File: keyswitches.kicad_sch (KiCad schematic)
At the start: 16 parts

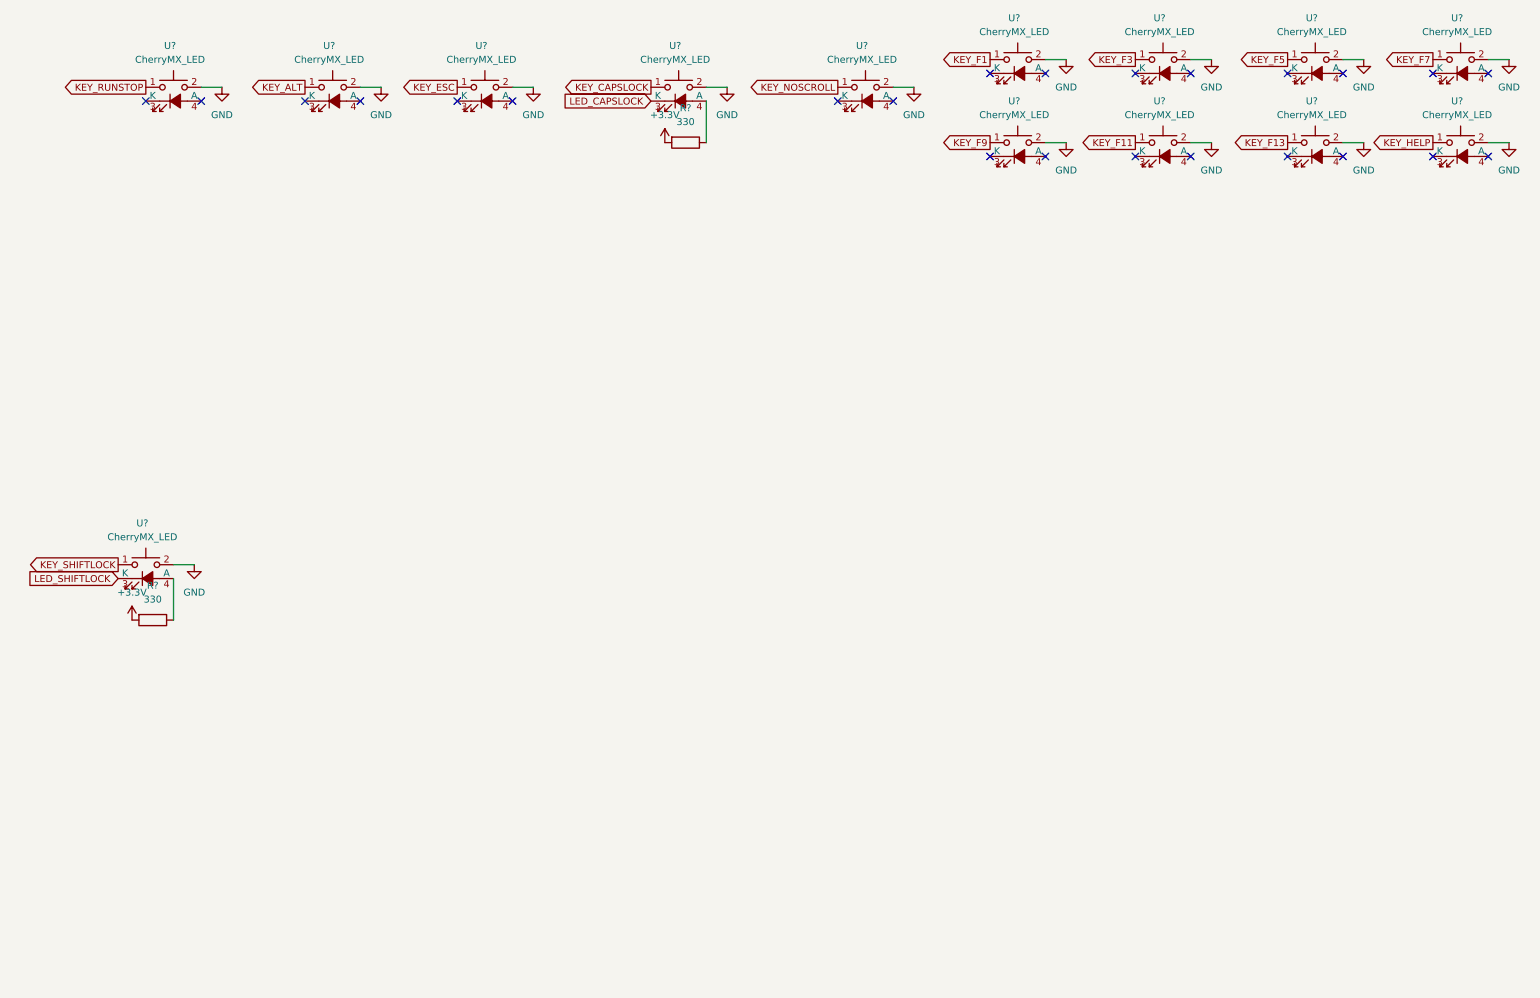
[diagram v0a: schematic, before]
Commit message: place top row of key switches
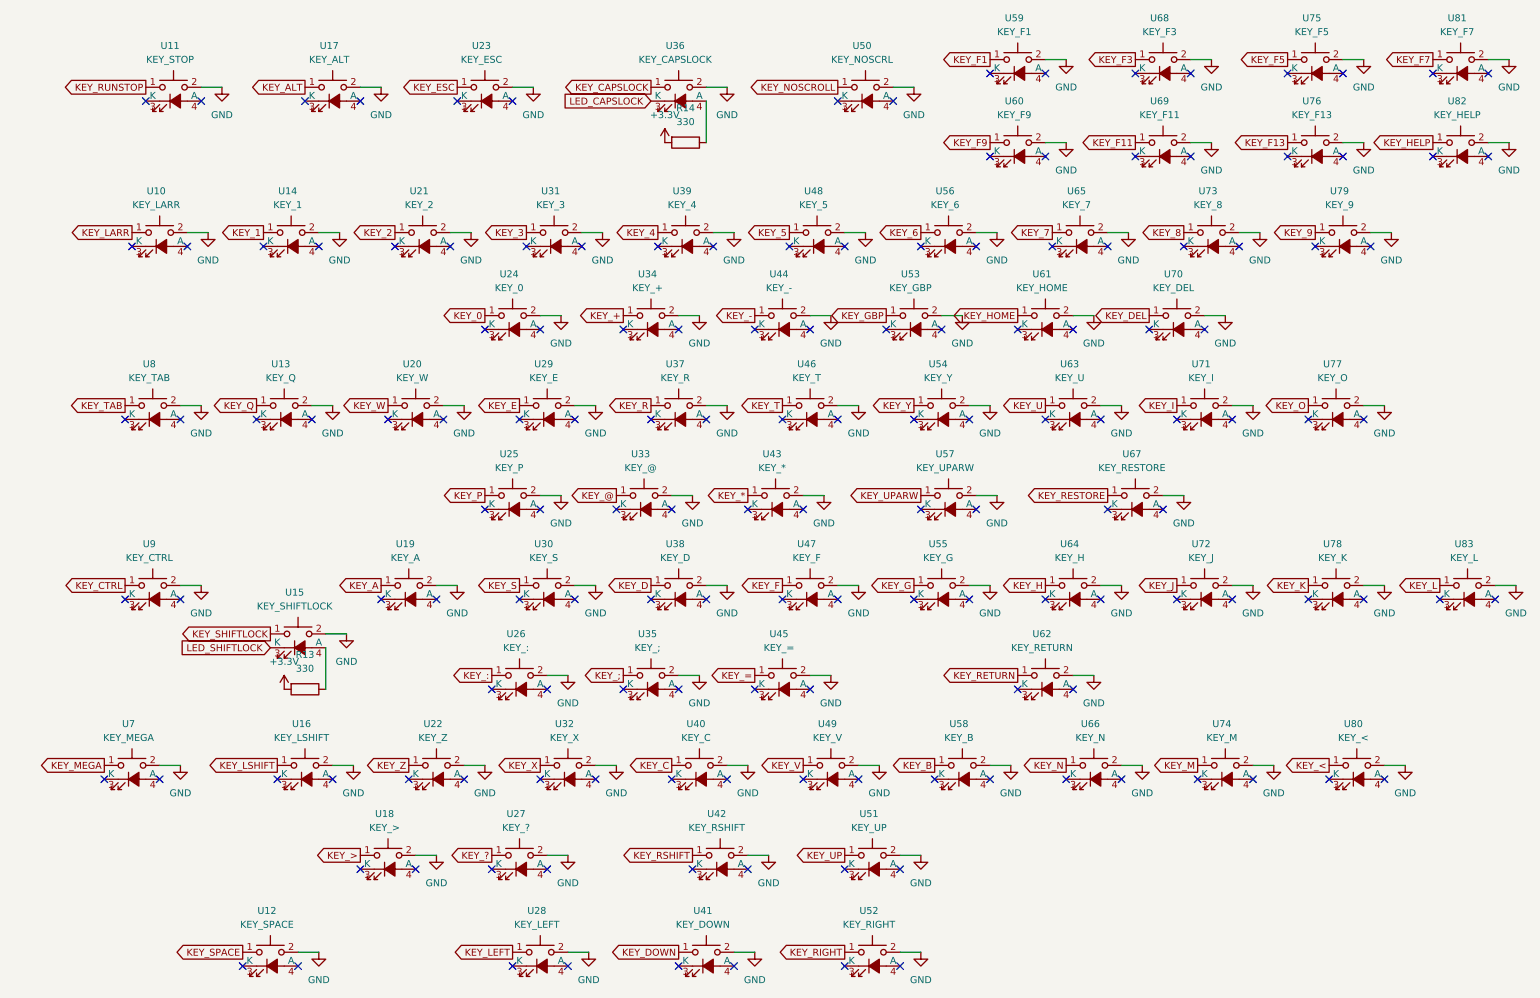
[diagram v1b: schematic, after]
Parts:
- added U10: KEY_LARR, 00Project-KeySwitches:SW_Cherry_MX1A_1.00u_PCB_LED, symbol 00Project-CherryMX:CherryMX_LED
- added U12: KEY_SPACE, 00Project-KeySwitches:SW_Cherry_MX1A_1.00u_PCB_LED, symbol 00Project-CherryMX:CherryMX_LED
- added U13: KEY_Q, 00Project-KeySwitches:SW_Cherry_MX1A_1.00u_PCB_LED, symbol 00Project-CherryMX:CherryMX_LED
- added U14: KEY_1, 00Project-KeySwitches:SW_Cherry_MX1A_1.00u_PCB_LED, symbol 00Project-CherryMX:CherryMX_LED
- added U16: KEY_LSHIFT, 00Project-KeySwitches:SW_Cherry_MX1A_1.00u_PCB_LED, symbol 00Project-CherryMX:CherryMX_LED
- added U18: KEY_>, 00Project-KeySwitches:SW_Cherry_MX1A_1.00u_PCB_LED, symbol 00Project-CherryMX:CherryMX_LED
- added U19: KEY_A, 00Project-KeySwitches:SW_Cherry_MX1A_1.00u_PCB_LED, symbol 00Project-CherryMX:CherryMX_LED
- added U20: KEY_W, 00Project-KeySwitches:SW_Cherry_MX1A_1.00u_PCB_LED, symbol 00Project-CherryMX:CherryMX_LED
- added U21: KEY_2, 00Project-KeySwitches:SW_Cherry_MX1A_1.00u_PCB_LED, symbol 00Project-CherryMX:CherryMX_LED
- added U22: KEY_Z, 00Project-KeySwitches:SW_Cherry_MX1A_1.00u_PCB_LED, symbol 00Project-CherryMX:CherryMX_LED
- added U24: KEY_0, 00Project-KeySwitches:SW_Cherry_MX1A_1.00u_PCB_LED, symbol 00Project-CherryMX:CherryMX_LED
- added U25: KEY_P, 00Project-KeySwitches:SW_Cherry_MX1A_1.00u_PCB_LED, symbol 00Project-CherryMX:CherryMX_LED
- added U26: KEY_:, 00Project-KeySwitches:SW_Cherry_MX1A_1.00u_PCB_LED, symbol 00Project-CherryMX:CherryMX_LED
- added U27: KEY_?, 00Project-KeySwitches:SW_Cherry_MX1A_1.00u_PCB_LED, symbol 00Project-CherryMX:CherryMX_LED
- added U28: KEY_LEFT, 00Project-KeySwitches:SW_Cherry_MX1A_1.00u_PCB_LED, symbol 00Project-CherryMX:CherryMX_LED
- added U29: KEY_E, 00Project-KeySwitches:SW_Cherry_MX1A_1.00u_PCB_LED, symbol 00Project-CherryMX:CherryMX_LED
- added U30: KEY_S, 00Project-KeySwitches:SW_Cherry_MX1A_1.00u_PCB_LED, symbol 00Project-CherryMX:CherryMX_LED
- added U31: KEY_3, 00Project-KeySwitches:SW_Cherry_MX1A_1.00u_PCB_LED, symbol 00Project-CherryMX:CherryMX_LED
- added U32: KEY_X, 00Project-KeySwitches:SW_Cherry_MX1A_1.00u_PCB_LED, symbol 00Project-CherryMX:CherryMX_LED
- added U33: KEY_@, 00Project-KeySwitches:SW_Cherry_MX1A_1.00u_PCB_LED, symbol 00Project-CherryMX:CherryMX_LED
- added U34: KEY_+, 00Project-KeySwitches:SW_Cherry_MX1A_1.00u_PCB_LED, symbol 00Project-CherryMX:CherryMX_LED
- added U35: KEY_;, 00Project-KeySwitches:SW_Cherry_MX1A_1.00u_PCB_LED, symbol 00Project-CherryMX:CherryMX_LED
- added U37: KEY_R, 00Project-KeySwitches:SW_Cherry_MX1A_1.00u_PCB_LED, symbol 00Project-CherryMX:CherryMX_LED
- added U38: KEY_D, 00Project-KeySwitches:SW_Cherry_MX1A_1.00u_PCB_LED, symbol 00Project-CherryMX:CherryMX_LED
- added U39: KEY_4, 00Project-KeySwitches:SW_Cherry_MX1A_1.00u_PCB_LED, symbol 00Project-CherryMX:CherryMX_LED
- added U40: KEY_C, 00Project-KeySwitches:SW_Cherry_MX1A_1.00u_PCB_LED, symbol 00Project-CherryMX:CherryMX_LED
- added U41: KEY_DOWN, 00Project-KeySwitches:SW_Cherry_MX1A_1.00u_PCB_LED, symbol 00Project-CherryMX:CherryMX_LED
- added U42: KEY_RSHIFT, 00Project-KeySwitches:SW_Cherry_MX1A_1.00u_PCB_LED, symbol 00Project-CherryMX:CherryMX_LED
- added U43: KEY_*, 00Project-KeySwitches:SW_Cherry_MX1A_1.00u_PCB_LED, symbol 00Project-CherryMX:CherryMX_LED
- added U44: KEY_-, 00Project-KeySwitches:SW_Cherry_MX1A_1.00u_PCB_LED, symbol 00Project-CherryMX:CherryMX_LED
- added U45: KEY_=, 00Project-KeySwitches:SW_Cherry_MX1A_1.00u_PCB_LED, symbol 00Project-CherryMX:CherryMX_LED
- added U46: KEY_T, 00Project-KeySwitches:SW_Cherry_MX1A_1.00u_PCB_LED, symbol 00Project-CherryMX:CherryMX_LED
- added U47: KEY_F, 00Project-KeySwitches:SW_Cherry_MX1A_1.00u_PCB_LED, symbol 00Project-CherryMX:CherryMX_LED
- added U48: KEY_5, 00Project-KeySwitches:SW_Cherry_MX1A_1.00u_PCB_LED, symbol 00Project-CherryMX:CherryMX_LED
- added U49: KEY_V, 00Project-KeySwitches:SW_Cherry_MX1A_1.00u_PCB_LED, symbol 00Project-CherryMX:CherryMX_LED
- added U51: KEY_UP, 00Project-KeySwitches:SW_Cherry_MX1A_1.00u_PCB_LED, symbol 00Project-CherryMX:CherryMX_LED
- added U52: KEY_RIGHT, 00Project-KeySwitches:SW_Cherry_MX1A_1.00u_PCB_LED, symbol 00Project-CherryMX:CherryMX_LED
- added U53: KEY_GBP, 00Project-KeySwitches:SW_Cherry_MX1A_1.00u_PCB_LED, symbol 00Project-CherryMX:CherryMX_LED
- added U54: KEY_Y, 00Project-KeySwitches:SW_Cherry_MX1A_1.00u_PCB_LED, symbol 00Project-CherryMX:CherryMX_LED
- added U55: KEY_G, 00Project-KeySwitches:SW_Cherry_MX1A_1.00u_PCB_LED, symbol 00Project-CherryMX:CherryMX_LED
- added U56: KEY_6, 00Project-KeySwitches:SW_Cherry_MX1A_1.00u_PCB_LED, symbol 00Project-CherryMX:CherryMX_LED
- added U57: KEY_UPARW, 00Project-KeySwitches:SW_Cherry_MX1A_1.00u_PCB_LED, symbol 00Project-CherryMX:CherryMX_LED
- added U58: KEY_B, 00Project-KeySwitches:SW_Cherry_MX1A_1.00u_PCB_LED, symbol 00Project-CherryMX:CherryMX_LED
- added U61: KEY_HOME, 00Project-KeySwitches:SW_Cherry_MX1A_1.00u_PCB_LED, symbol 00Project-CherryMX:CherryMX_LED
- added U62: KEY_RETURN, 00Project-KeySwitches:SW_Cherry_MX1A_1.00u_PCB_LED, symbol 00Project-CherryMX:CherryMX_LED
- added U63: KEY_U, 00Project-KeySwitches:SW_Cherry_MX1A_1.00u_PCB_LED, symbol 00Project-CherryMX:CherryMX_LED
- added U64: KEY_H, 00Project-KeySwitches:SW_Cherry_MX1A_1.00u_PCB_LED, symbol 00Project-CherryMX:CherryMX_LED
- added U65: KEY_7, 00Project-KeySwitches:SW_Cherry_MX1A_1.00u_PCB_LED, symbol 00Project-CherryMX:CherryMX_LED
- added U66: KEY_N, 00Project-KeySwitches:SW_Cherry_MX1A_1.00u_PCB_LED, symbol 00Project-CherryMX:CherryMX_LED
- added U67: KEY_RESTORE, 00Project-KeySwitches:SW_Cherry_MX1A_1.00u_PCB_LED, symbol 00Project-CherryMX:CherryMX_LED
- added U7: KEY_MEGA, 00Project-KeySwitches:SW_Cherry_MX1A_1.00u_PCB_LED, symbol 00Project-CherryMX:CherryMX_LED
- added U70: KEY_DEL, 00Project-KeySwitches:SW_Cherry_MX1A_1.00u_PCB_LED, symbol 00Project-CherryMX:CherryMX_LED
- added U71: KEY_I, 00Project-KeySwitches:SW_Cherry_MX1A_1.00u_PCB_LED, symbol 00Project-CherryMX:CherryMX_LED
- added U72: KEY_J, 00Project-KeySwitches:SW_Cherry_MX1A_1.00u_PCB_LED, symbol 00Project-CherryMX:CherryMX_LED
- added U73: KEY_8, 00Project-KeySwitches:SW_Cherry_MX1A_1.00u_PCB_LED, symbol 00Project-CherryMX:CherryMX_LED
- added U74: KEY_M, 00Project-KeySwitches:SW_Cherry_MX1A_1.00u_PCB_LED, symbol 00Project-CherryMX:CherryMX_LED
- added U77: KEY_O, 00Project-KeySwitches:SW_Cherry_MX1A_1.00u_PCB_LED, symbol 00Project-CherryMX:CherryMX_LED
- added U78: KEY_K, 00Project-KeySwitches:SW_Cherry_MX1A_1.00u_PCB_LED, symbol 00Project-CherryMX:CherryMX_LED
- added U79: KEY_9, 00Project-KeySwitches:SW_Cherry_MX1A_1.00u_PCB_LED, symbol 00Project-CherryMX:CherryMX_LED
- added U8: KEY_TAB, 00Project-KeySwitches:SW_Cherry_MX1A_1.00u_PCB_LED, symbol 00Project-CherryMX:CherryMX_LED
- added U80: KEY_<, 00Project-KeySwitches:SW_Cherry_MX1A_1.00u_PCB_LED, symbol 00Project-CherryMX:CherryMX_LED
- added U83: KEY_L, 00Project-KeySwitches:SW_Cherry_MX1A_1.00u_PCB_LED, symbol 00Project-CherryMX:CherryMX_LED
- added U9: KEY_CTRL, 00Project-KeySwitches:SW_Cherry_MX1A_1.00u_PCB_LED, symbol 00Project-CherryMX:CherryMX_LED
- U11: renamed from U?; value CherryMX_LED -> KEY_STOP
- U15: renamed from U?; value CherryMX_LED -> KEY_SHIFTLOCK
- U17: renamed from U?; value CherryMX_LED -> KEY_ALT
- U23: renamed from U?; value CherryMX_LED -> KEY_ESC
- U36: renamed from U?; value CherryMX_LED -> KEY_CAPSLOCK
- U50: renamed from U?; value CherryMX_LED -> KEY_NOSCRL
- U59: renamed from U?; value CherryMX_LED -> KEY_F1
- U60: renamed from U?; value CherryMX_LED -> KEY_F9
- U68: renamed from U?; value CherryMX_LED -> KEY_F3
- U69: renamed from U?; value CherryMX_LED -> KEY_F11
- U75: renamed from U?; value CherryMX_LED -> KEY_F5
- U76: renamed from U?; value CherryMX_LED -> KEY_F13
- U81: renamed from U?; value CherryMX_LED -> KEY_F7
- U82: renamed from U?; value CherryMX_LED -> KEY_HELP
- gave numbers to parts that had none: 2
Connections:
- net GND: now also U10.2, U12.2, U13.2, U14.2, U16.2, U18.2, U19.2, U20.2, U21.2, U22.2, U24.2, U25.2, U26.2, U27.2, U28.2, U29.2, U30.2, U31.2, U32.2, U33.2, U34.2, U35.2, U37.2, U38.2, U39.2, U40.2, U41.2, U42.2, U43.2, U44.2, U45.2, U46.2, U47.2, U48.2, U49.2, U51.2, U52.2, U53.2, U54.2, U55.2, U56.2, U57.2, U58.2, U61.2, U62.2, U63.2, U64.2, U65.2, U66.2, U67.2, U7.2, U70.2, U71.2, U72.2, U73.2, U74.2, U77.2, U78.2, U79.2, U8.2, U80.2, U83.2, U9.2
- new net KEY_*: U43.1
- new net KEY_+: U34.1
- new net KEY_-: U44.1
- new net KEY_0: U24.1
- new net KEY_1: U14.1
- new net KEY_2: U21.1
- new net KEY_3: U31.1
- new net KEY_4: U39.1
- new net KEY_5: U48.1
- new net KEY_6: U56.1
- new net KEY_7: U65.1
- new net KEY_8: U73.1
- new net KEY_9: U79.1
- new net KEY_:: U26.1
- new net KEY_;: U35.1
- new net KEY_<: U80.1
- new net KEY_=: U45.1
- new net KEY_>: U18.1
- new net KEY_?: U27.1
- new net KEY_@: U33.1
- new net KEY_A: U19.1
- new net KEY_B: U58.1
- new net KEY_C: U40.1
- new net KEY_CTRL: U9.1
- new net KEY_D: U38.1
- new net KEY_DEL: U70.1
- new net KEY_DOWN: U41.1
- new net KEY_E: U29.1
- new net KEY_F: U47.1
- new net KEY_G: U55.1
- new net KEY_GBP: U53.1
- new net KEY_H: U64.1
- new net KEY_HOME: U61.1
- new net KEY_I: U71.1
- new net KEY_J: U72.1
- new net KEY_K: U78.1
- new net KEY_L: U83.1
- new net KEY_LARR: U10.1
- new net KEY_LEFT: U28.1
- new net KEY_LSHIFT: U16.1
- new net KEY_M: U74.1
- new net KEY_MEGA: U7.1
- new net KEY_N: U66.1
- new net KEY_O: U77.1
- new net KEY_P: U25.1
- new net KEY_Q: U13.1
- new net KEY_R: U37.1
- new net KEY_RESTORE: U67.1
- new net KEY_RETURN: U62.1
- new net KEY_RIGHT: U52.1
- new net KEY_RSHIFT: U42.1
- new net KEY_S: U30.1
- new net KEY_SPACE: U12.1
- new net KEY_T: U46.1
- new net KEY_TAB: U8.1
- new net KEY_U: U63.1
- new net KEY_UP: U51.1
- new net KEY_UPARW: U57.1
- new net KEY_V: U49.1
- new net KEY_W: U20.1
- new net KEY_X: U32.1
- new net KEY_Y: U54.1
- new net KEY_Z: U22.1
- no-connect marks 24 -> 150
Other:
- moved on the sheet: R13, U15

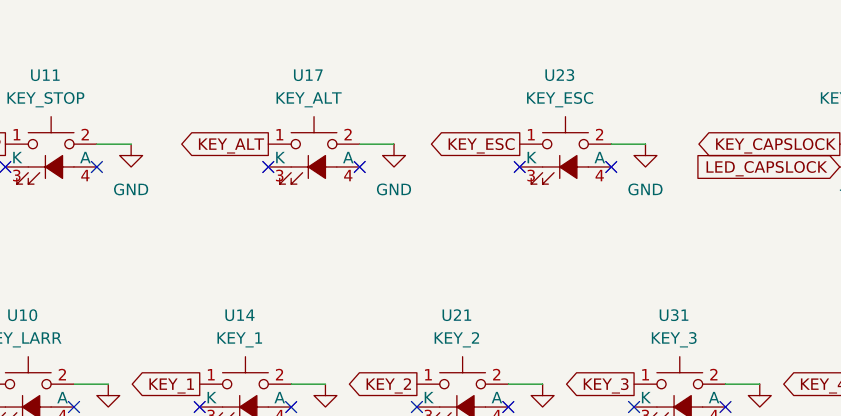
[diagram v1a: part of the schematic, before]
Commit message: add and place mounting holes
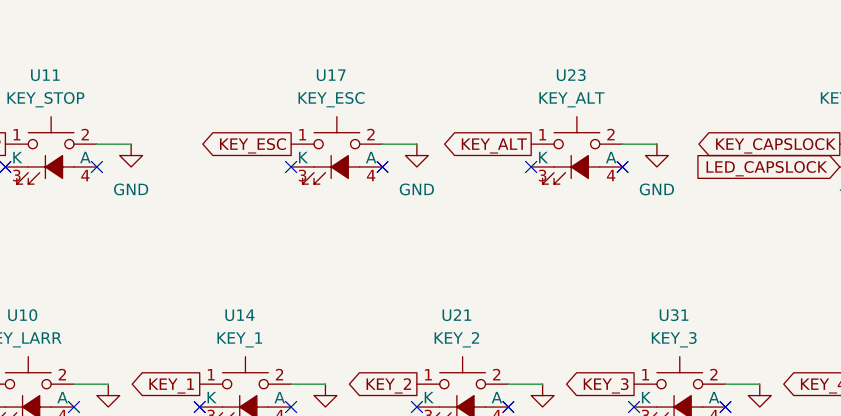
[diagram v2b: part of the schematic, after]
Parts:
- renumbered U23 to U17, U17 to U23
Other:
- moved on the sheet: U17, U23
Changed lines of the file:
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@@
   (no_connect (at 173.99 156.21))
   (no_connect (at 82.55 123.19))
-  (no_connect (at 86.36 31.75))
+  (no_connect (at 60.96 31.75))
   (no_connect (at 276.86 123.19))
   (no_connect (at 140.97 139.7))
@@
   (no_connect (at 170.18 123.19))
   (no_connect (at 228.6 123.19))
-  (no_connect (at 58.42 31.75))
-  (no_connect (at 68.58 31.75))
+  (no_connect (at 87.63 31.75))
+  (no_connect (at 97.79 31.75))
   (no_connect (at 189.23 139.7))
   (no_connect (at 184.15 156.21))
@@
   (no_connect (at 215.9 106.68))
   (no_connect (at 53.34 156.21))
-  (no_connect (at 96.52 31.75))
+  (no_connect (at 71.12 31.75))
   (no_connect (at 181.61 58.42))
   (no_connect (at 139.7 172.72))
@@
     (stroke (width 0) (type default) (color 0 0 0 0))
   )
-  (wire (pts (xy 96.52 29.21) (xy 100.33 29.21))
+  (wire (pts (xy 71.12 29.21) (xy 74.93 29.21))
     (stroke (width 0) (type default) (color 0 0 0 0))
   )
@@
     (stroke (width 0) (type default) (color 0 0 0 0))
   )
-  (wire (pts (xy 68.58 29.21) (xy 72.39 29.21))
+  (wire (pts (xy 97.79 29.21) (xy 101.6 29.21))
     (stroke (width 0) (type default) (color 0 0 0 0))
   )
@@
     )
   )
-  (global_label "KEY_ESC" (shape output) (at 86.36 29.21 180) (fields_autoplaced)
-    (effects (font (size 1.27 1.27)) (justify right))
-    (property "Intersheet References" "${INTERSHEET_REFS}" (id 0) (at 75.8431 29.1306 0)
+  (global_label "KEY_ESC" (shape output) (at 60.96 29.21 180) (fields_autoplaced)
+    (effects (font (size 1.27 1.27)) (justify right))
+    (property "Intersheet References" "${INTERSHEET_REFS}" (id 0) (at 50.4431 29.1306 0)
       (effects (font (size 1.27 1.27)) (justify right) hide)
     )
@@
     )
   )
-  (global_label "KEY_ALT" (shape output) (at 58.42 29.21 180) (fields_autoplaced)
-    (effects (font (size 1.27 1.27)) (justify right))
-    (property "Intersheet References" "${INTERSHEET_REFS}" (id 0) (at 48.4474 29.1306 0)
+  (global_label "KEY_ALT" (shape output) (at 87.63 29.21 180) (fields_autoplaced)
+    (effects (font (size 1.27 1.27)) (justify right))
+    (property "Intersheet References" "${INTERSHEET_REFS}" (id 0) (at 77.6574 29.1306 0)
       (effects (font (size 1.27 1.27)) (justify right) hide)
     )
@@
     (pin "1")
   )
-  (symbol (lib_id "00Project-CherryMX:CherryMX_LED") (at 63.5 30.48 0) (unit 1)
-    (in_bom yes) (on_board yes) (fields_autoplaced)
-    (property "Reference" "U17" (id 0) (at 62.865 21.59 0))
-    (property "Value" "KEY_ALT" (id 1) (at 62.865 24.13 0))
-    (property "Footprint" "00Project-KeySwitches:SW_Cherry_MX1A_1.00u_PCB_LED" (id 2) (at 63.5 30.48 0)
-      (effects (font (size 1.27 1.27)) hide)
-    )
-    (property "Datasheet" "" (id 3) (at 63.5 30.48 0)
+  (symbol (lib_id "00Project-CherryMX:CherryMX_LED") (at 92.71 30.48 0) (unit 1)
+    (in_bom yes) (on_board yes) (fields_autoplaced)
+    (property "Reference" "U23" (id 0) (at 92.075 21.59 0))
+    (property "Value" "KEY_ALT" (id 1) (at 92.075 24.13 0))
+    (property "Footprint" "00Project-KeySwitches:SW_Cherry_MX1A_1.00u_PCB_LED" (id 2) (at 92.71 30.48 0)
+      (effects (font (size 1.27 1.27)) hide)
+    )
+    (property "Datasheet" "" (id 3) (at 92.71 30.48 0)
       (effects (font (size 1.27 1.27)) hide)
     )
@@
     (pin "4")
   )
-  (symbol (lib_id "power:GND") (at 72.39 29.21 0) (unit 1)
-    (in_bom yes) (on_board yes) (fields_autoplaced)
-    (property "Reference" "#PWR042" (id 0) (at 72.39 35.56 0)
-      (effects (font (size 1.27 1.27)) hide)
-    )
-    (property "Value" "GND" (id 1) (at 72.39 34.29 0))
-    (property "Footprint" "" (id 2) (at 72.39 29.21 0)
-      (effects (font (size 1.27 1.27)) hide)
-    )
-    (property "Datasheet" "" (id 3) (at 72.39 29.21 0)
+  (symbol (lib_id "power:GND") (at 101.6 29.21 0) (unit 1)
+    (in_bom yes) (on_board yes) (fields_autoplaced)
+    (property "Reference" "#PWR048" (id 0) (at 101.6 35.56 0)
+      (effects (font (size 1.27 1.27)) hide)
+    )
+    (property "Value" "GND" (id 1) (at 101.6 34.29 0))
+    (property "Footprint" "" (id 2) (at 101.6 29.21 0)
+      (effects (font (size 1.27 1.27)) hide)
+    )
+    (property "Datasheet" "" (id 3) (at 101.6 29.21 0)
       (effects (font (size 1.27 1.27)) hide)
     )
@@
     (pin "1")
   )
-  (symbol (lib_id "power:GND") (at 100.33 29.21 0) (unit 1)
-    (in_bom yes) (on_board yes) (fields_autoplaced)
-    (property "Reference" "#PWR048" (id 0) (at 100.33 35.56 0)
-      (effects (font (size 1.27 1.27)) hide)
-    )
-    (property "Value" "GND" (id 1) (at 100.33 34.29 0))
-    (property "Footprint" "" (id 2) (at 100.33 29.21 0)
-      (effects (font (size 1.27 1.27)) hide)
-    )
-    (property "Datasheet" "" (id 3) (at 100.33 29.21 0)
+  (symbol (lib_id "power:GND") (at 74.93 29.21 0) (unit 1)
+    (in_bom yes) (on_board yes) (fields_autoplaced)
+    (property "Reference" "#PWR042" (id 0) (at 74.93 35.56 0)
+      (effects (font (size 1.27 1.27)) hide)
+    )
+    (property "Value" "GND" (id 1) (at 74.93 34.29 0))
+    (property "Footprint" "" (id 2) (at 74.93 29.21 0)
+      (effects (font (size 1.27 1.27)) hide)
+    )
+    (property "Datasheet" "" (id 3) (at 74.93 29.21 0)
       (effects (font (size 1.27 1.27)) hide)
     )
@@
     (pin "1")
   )
-  (symbol (lib_id "00Project-CherryMX:CherryMX_LED") (at 91.44 30.48 0) (unit 1)
-    (in_bom yes) (on_board yes) (fields_autoplaced)
-    (property "Reference" "U23" (id 0) (at 90.805 21.59 0))
-    (property "Value" "KEY_ESC" (id 1) (at 90.805 24.13 0))
-    (property "Footprint" "00Project-KeySwitches:SW_Cherry_MX1A_1.00u_PCB_LED" (id 2) (at 91.44 30.48 0)
-      (effects (font (size 1.27 1.27)) hide)
-    )
-    (property "Datasheet" "" (id 3) (at 91.44 30.48 0)
-      (effects (font (size 1.27 1.27)) hide)
-    )
+  (symbol (lib_id "00Project-CherryMX:CherryMX_LED") (at 66.04 30.48 0) (unit 1)
+    (in_bom yes) (on_board yes) (fields_autoplaced)
+    (property "Reference" "U17" (id 0) (at 65.405 21.59 0))
+    (property "Value" "KEY_ESC" (id 1) (at 65.405 24.13 0))
+    (property "Footprint" "00Project-KeySwitches:SW_Cherry_MX1A_1.00u_PCB_LED" (id 2) (at 66.04 30.48 0)
+      (effects (font (size 1.27 1.27)) hide)
+    )
+    (property "Datasheet" "" (id 3) (at 66.04 30.48 0)
+      (effects (font (size 1.27 1.27)) hide)
+    )

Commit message: finish placing LEDs and resistors
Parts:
- R13, R14: footprint (none) -> 00Project-LEDs:Labeled Resistor
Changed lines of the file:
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@@
     (property "Reference" "R13" (id 0) (at 58.42 133.35 90))
     (property "Value" "330" (id 1) (at 58.42 135.89 90))
-    (property "Footprint" "" (id 2) (at 58.42 137.922 90)
+    (property "Footprint" "00Project-LEDs:Labeled Resistor" (id 2) (at 58.42 137.922 90)
       (effects (font (size 1.27 1.27)) hide)
     )
@@
     (property "Reference" "R14" (id 0) (at 128.27 33.02 90))
     (property "Value" "330" (id 1) (at 128.27 35.56 90))
-    (property "Footprint" "" (id 2) (at 128.27 37.592 90)
+    (property "Footprint" "00Project-LEDs:Labeled Resistor" (id 2) (at 128.27 37.592 90)
       (effects (font (size 1.27 1.27)) hide)
     )

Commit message: finish adding missing I2C pull-ups
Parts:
- renumbered R13 to R15, R14 to R16

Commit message: fix all DRC warnings. begin adding pin 1 SMD markers
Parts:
- U62: footprint 00Project-KeySwitches:SW_Cherry_MX1A_1.00u_PCB_LED -> 00Project-KeySwitches:SW_Cherry_MX1A_2.00u_PCB
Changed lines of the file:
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@@
     (property "Reference" "U62" (id 0) (at 193.675 129.54 0))
     (property "Value" "KEY_RETURN" (id 1) (at 193.675 132.08 0))
-    (property "Footprint" "00Project-KeySwitches:SW_Cherry_MX1A_1.00u_PCB_LED" (id 2) (at 194.31 138.43 0)
+    (property "Footprint" "00Project-KeySwitches:SW_Cherry_MX1A_2.00u_PCB" (id 2) (at 194.31 138.43 0)
       (effects (font (size 1.27 1.27)) hide)
     )
